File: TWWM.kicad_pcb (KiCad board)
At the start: 2 copper layers, 38 x 100.1 mm, 58 parts, among them J101 USB_B_Micro, J102 Molex 51021-0200, J103 Conn_01x10_Male, J104 Conn_01x10_Male, J105 18650, Q101 Q_NPN_BEC, Q102 Q_NPN_BEC, Q103 Q_NPN_BEC, Q104 Q_PMOS_GSD, SW101 SW_Push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

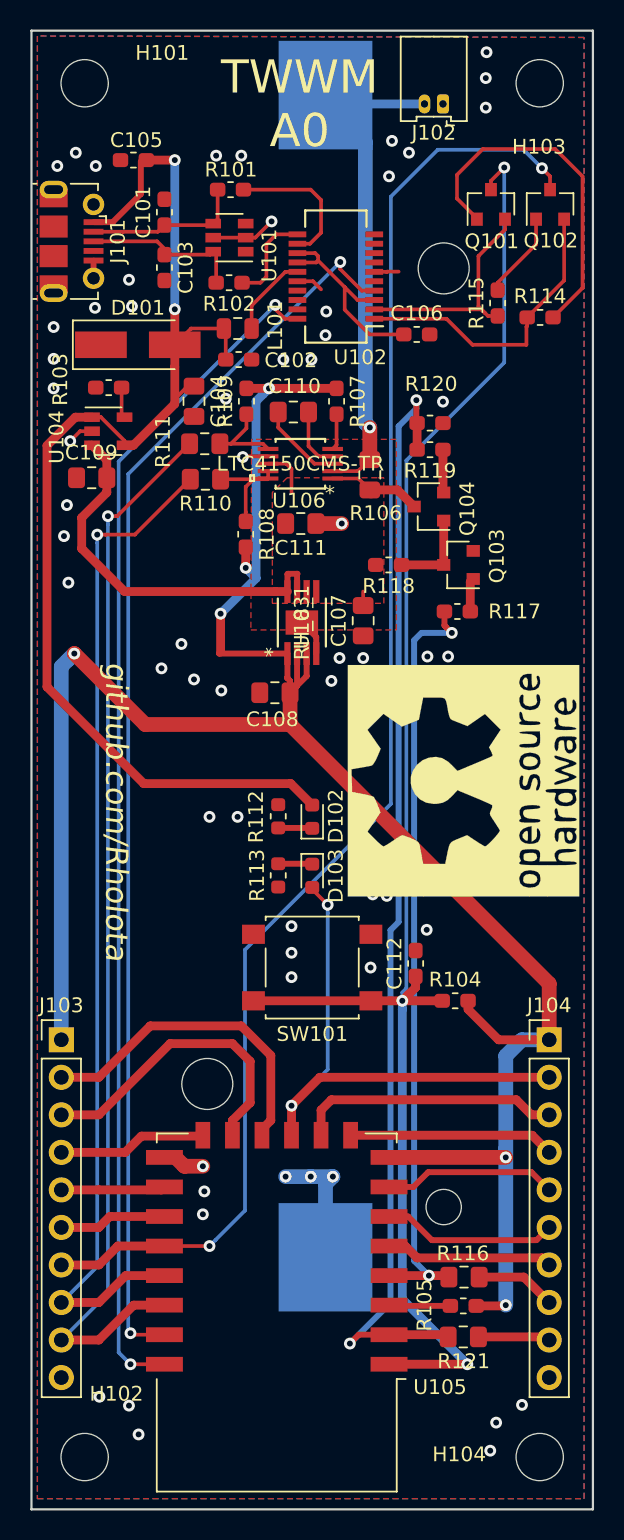
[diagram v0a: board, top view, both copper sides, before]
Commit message: -mod: update from A0 to A1: switched Tx and Rx. 10k pullup to GPIO0, 10k pulldown to GPIO15
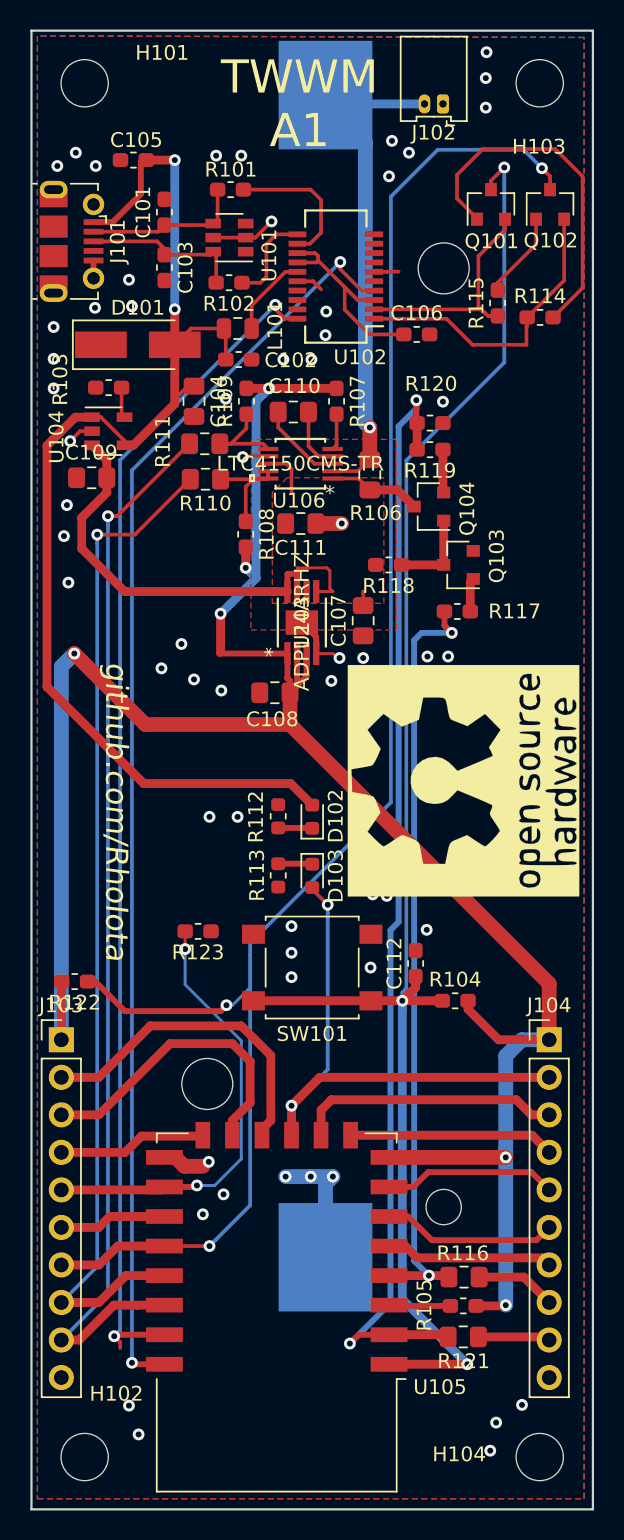
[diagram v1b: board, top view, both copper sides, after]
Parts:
- added R122: 10k, Resistor_SMD:R_0603_1608Metric_Pad1.05x0.95mm_HandSolder, F.Cu at (135.5, 114.0)
- added R123: 10k, Resistor_SMD:R_0603_1608Metric_Pad1.05x0.95mm_HandSolder, F.Cu at (143.9, 110.6)
- U103: value RH_8_1 -> ADP124ARHZ
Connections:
- U105 pad 21: /UART_RX -> /UART_TX
- U105 pad 22: /UART_TX -> /UART_RX
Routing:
- net /GPIO15: track 7.06 -> 31.0 mm, vias 0 -> 2
- net /GPIO0: track 100.4 -> 115.1 mm, vias 2 -> 3
- net +BATT: track 38.5 -> 45.0 mm
- net +3V3: track 152.0 -> 156.0 mm
- net /UART_RX: track 84.2 -> 86.0 mm
- net GND: track 28.6 -> 30.3 mm, vias 60 -> 59
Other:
- board text added: "TWWM A1"
- board text removed: "TWWM A0"
